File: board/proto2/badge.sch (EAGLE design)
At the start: 56 parts, among them IC1 TLV62569, J1 5051101092

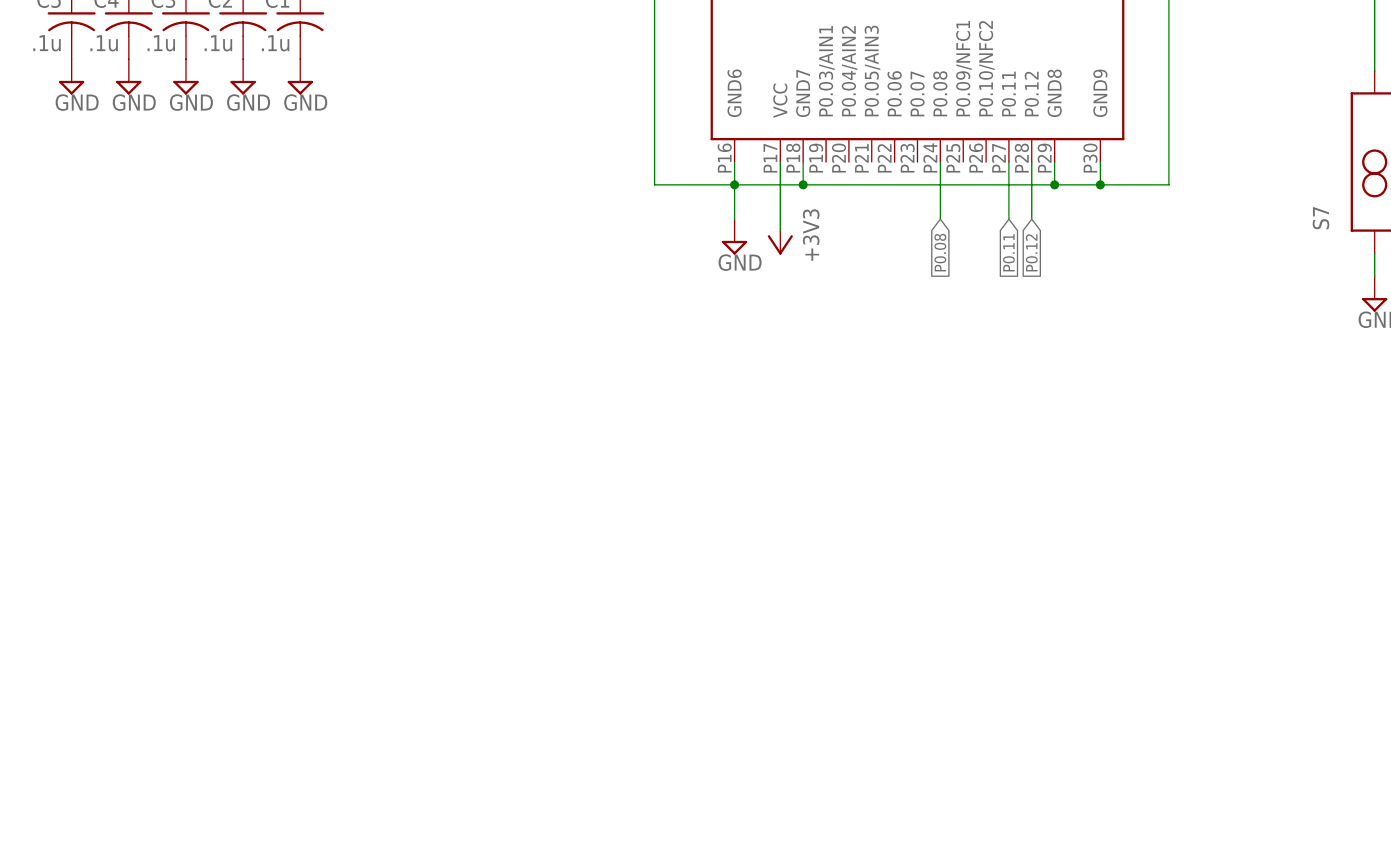
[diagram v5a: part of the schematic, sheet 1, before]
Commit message: added SD card holder to schematic
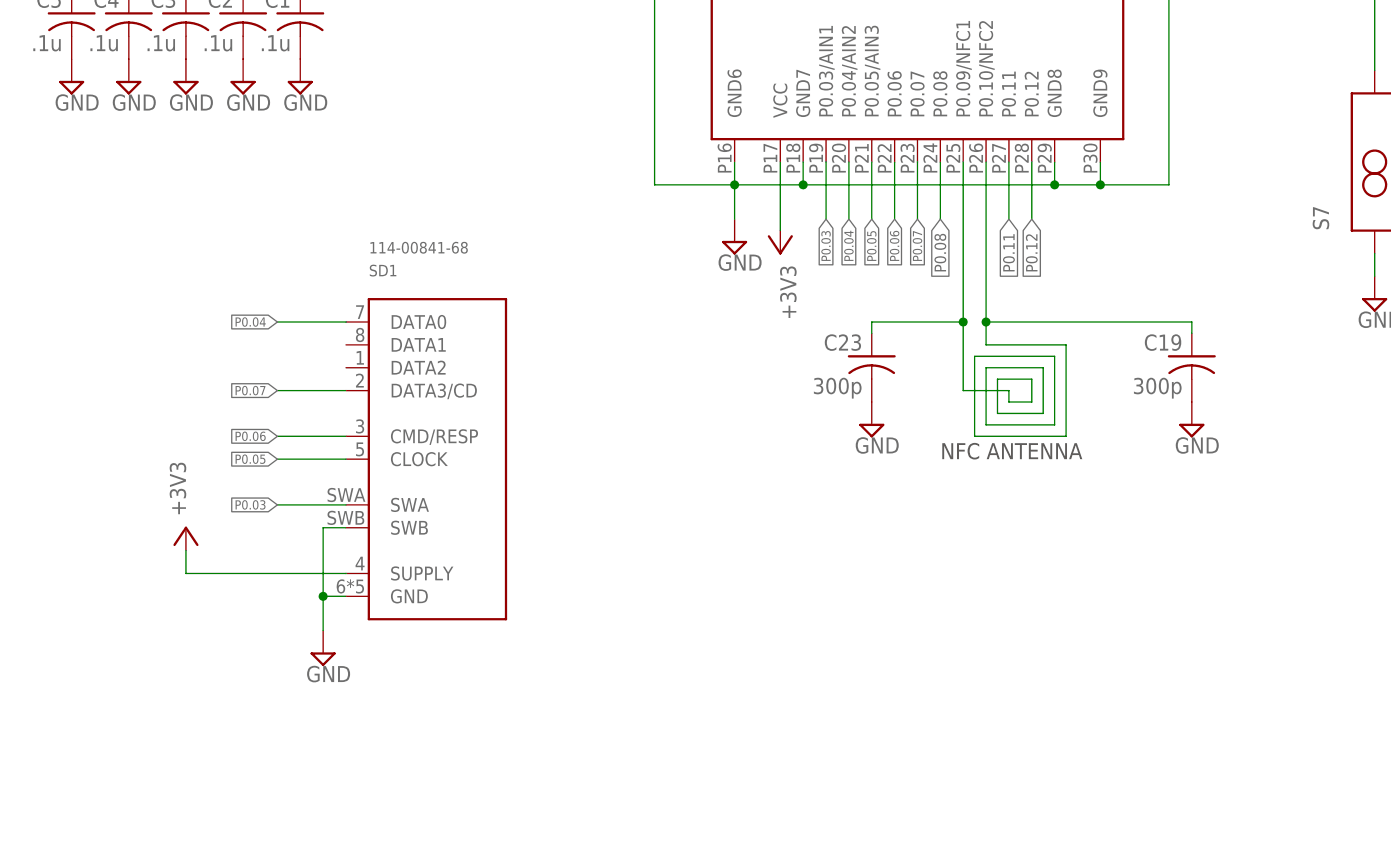
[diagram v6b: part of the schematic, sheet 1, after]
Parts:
- added C19, C23: 300p, rcl:C-USC0603K
- added SD1: 114-00841-68, badge:114-00841-68
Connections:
- new net ANT: C19.1, C23.1, U1.P0.09/NFC1, U1.P0.10/NFC2
- new net P0.03: SD1.SWA, U1.P0.03/AIN1
- new net P0.04: SD1.DATA0, U1.P0.04/AIN2
- new net P0.05: SD1.CLOCK, U1.P0.05/AIN3
- new net P0.06: SD1.CMD/RESP, U1.P0.06
- new net P0.07: SD1.DATA3/CD, U1.P0.07
- net +3V3: now also SD1.SUPPLY
- net GND: now also C19.2, C23.2, SD1.GND, SD1.SWB
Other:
- note added: "NFC ANTENNA"
